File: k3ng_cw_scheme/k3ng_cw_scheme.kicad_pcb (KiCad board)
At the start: 2 copper layers, 100 x 116.8 mm, 35 parts, among them J1 INPUT KEY, J2 OUTPUT KEY/PTT, SW1 CMD, SW2 MEM1, SW3 MEM2, SW4 MEM3, SW5 MEM4, U1 PC817, U2 PC817

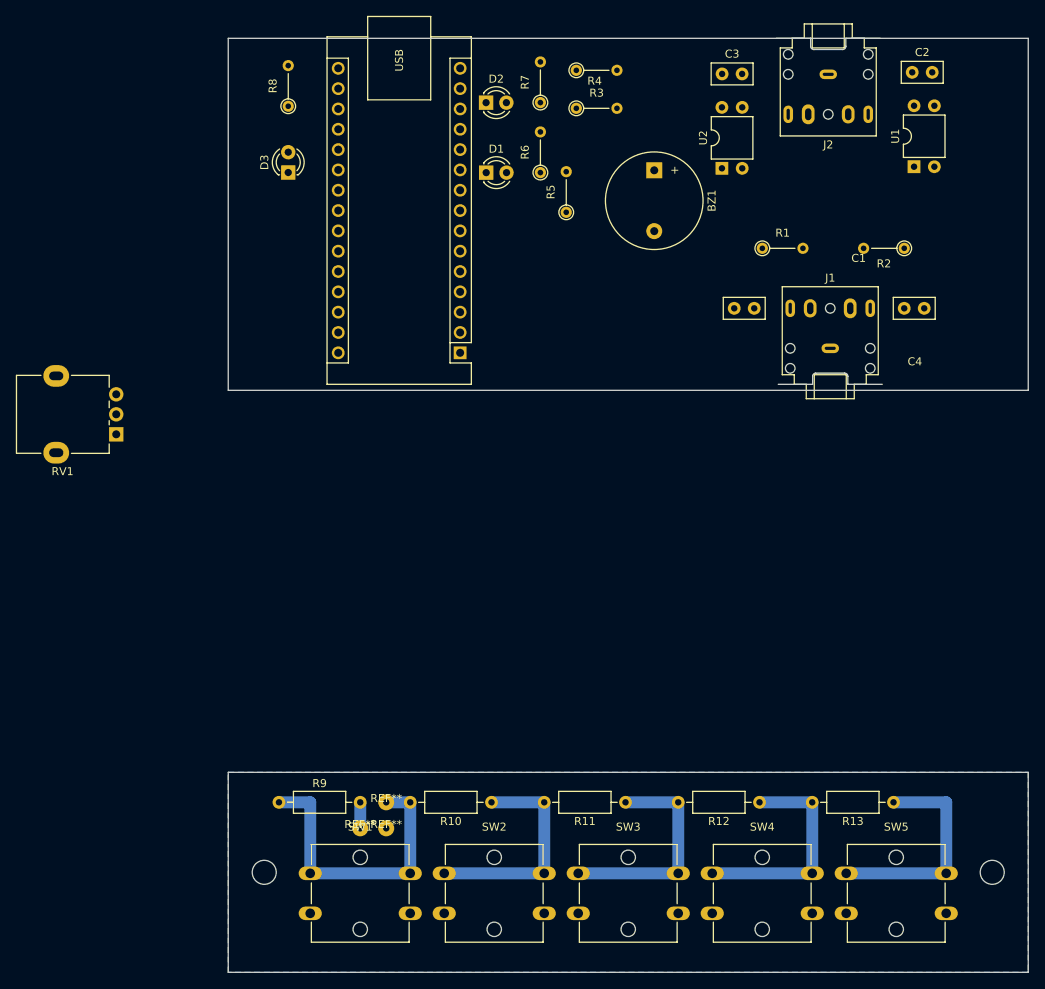
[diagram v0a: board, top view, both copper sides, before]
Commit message: Add keyboard connector Start working on PCB
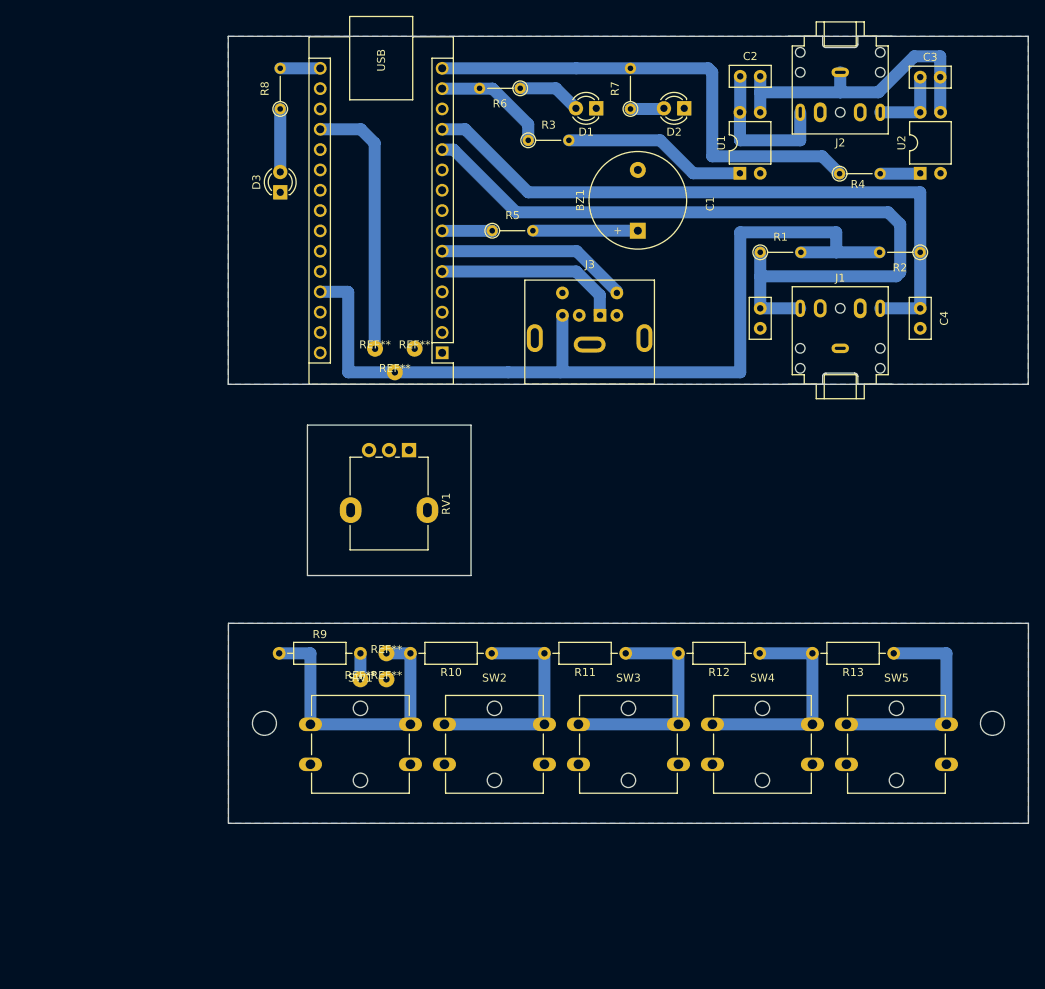
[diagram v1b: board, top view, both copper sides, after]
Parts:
- added J3: Keyboard, Footprints:Connector_Mini-DIN_Female_6Pin_2rows, F.Cu at (93.2, 98.6)
- added REF**: my_pad, my_lib:my_pad, F.Cu at (67.6, 105.8)
- added REF**: my_pad, my_lib:my_pad, F.Cu at (70.0, 102.8)
- added REF**: my_pad, my_lib:my_pad, F.Cu at (65.1, 102.8)
- moved RV1 36.7 mm to (69.3, 115.5), turned to -90 degrees
- moved R4 35.4 mm to (123.2, 80.9)
- moved U2 24.8 mm to (133.2, 80.9)
- moved D2 24.8 mm to (103.8, 72.8), turned to 180 degrees
- moved C3 24.8 mm to (133.2, 68.8)
- moved U1 21.8 mm to (110.7, 80.9)
- moved C2 21.5 mm to (110.8, 68.8)
- moved R10 18.6 mm to (79.7, 140.9)
- moved R11 18.6 mm to (96.4, 140.9)
- moved R12 18.6 mm to (113.2, 140.9)
- moved R13 18.6 mm to (129.9, 140.9)
- moved R9 18.6 mm to (53.1, 140.9)
- moved REF** 18.6 mm to (66.5, 144.1)
- moved REF** 18.6 mm to (66.5, 140.9)
- moved REF** 18.6 mm to (63.3, 144.1)
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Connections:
- A1 pad 11: unconnected-(A1-D8-Pad11) -> Net-(A1-D8)
- A1 pad 12: unconnected-(A1-D9-Pad12) -> Net-(A1-D9)
- C1 pad 1: Net-(A1-D3) -> Net-(A1-D8)
- C4 pad 1: Net-(A1-D2) -> Net-(A1-D9)
- J1 pad R: Net-(A1-D3) -> Net-(A1-D8)
- J1 pad T: Net-(A1-D2) -> Net-(A1-D9)
- J2 pad R: Net-(C2-Pad1) -> Net-(C3-Pad1)
- J2 pad T: Net-(C3-Pad1) -> Net-(C2-Pad1)
- R1 pad 1: Net-(A1-D3) -> Net-(A1-D8)
- R2 pad 1: Net-(A1-D2) -> Net-(A1-D9)
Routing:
- net +5V: track 3.25 -> 114.5 mm
- net Net-(A1-D8): track 0.00 -> 96.8 mm
- net Net-(A1-D9): track 0.00 -> 82.5 mm
- net Net-(A1-D12): track 0.00 -> 61.3 mm
- net Net-(C2-Pad2): track 0.00 -> 38.4 mm
- net Net-(A1-A0): track 0.00 -> 33.2 mm
- net Net-(A1-D3): track 0.00 -> 24.1 mm
- net Net-(A1-D2): track 0.00 -> 23.5 mm
- net Net-(R3-Pad2): track 0.00 -> 23.1 mm
- net Net-(C2-Pad1): track 0.00 -> 19.0 mm
- net Net-(A1-D11): track 0.00 -> 14.6 mm
- net Net-(BZ1-+): track 0.00 -> 13.1 mm
- net Net-(C3-Pad1): track 0.00 -> 9.40 mm
- net Net-(D1-A): track 0.00 -> 8.00 mm
- net Net-(D3-A): track 0.00 -> 7.88 mm
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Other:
- board size 100 x 116.8 mm -> 100 x 98.4 mm

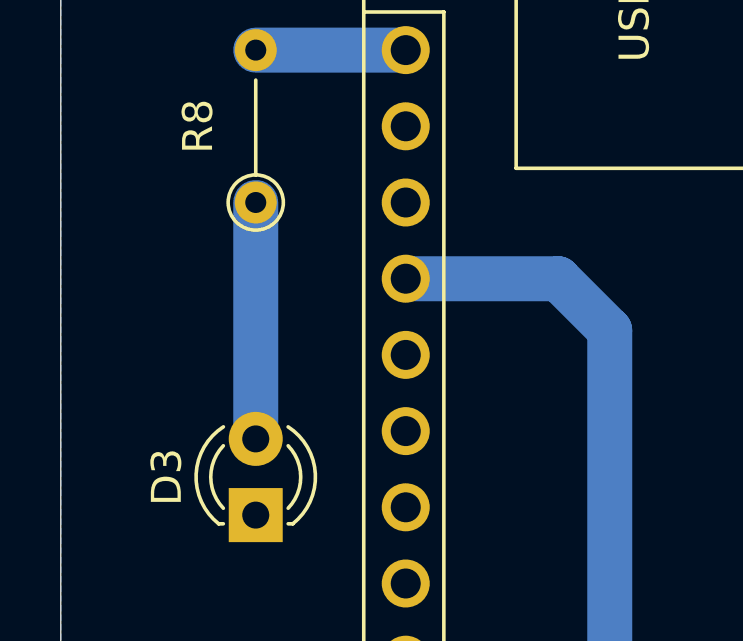
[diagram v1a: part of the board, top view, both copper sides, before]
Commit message: Add some pads to pcb
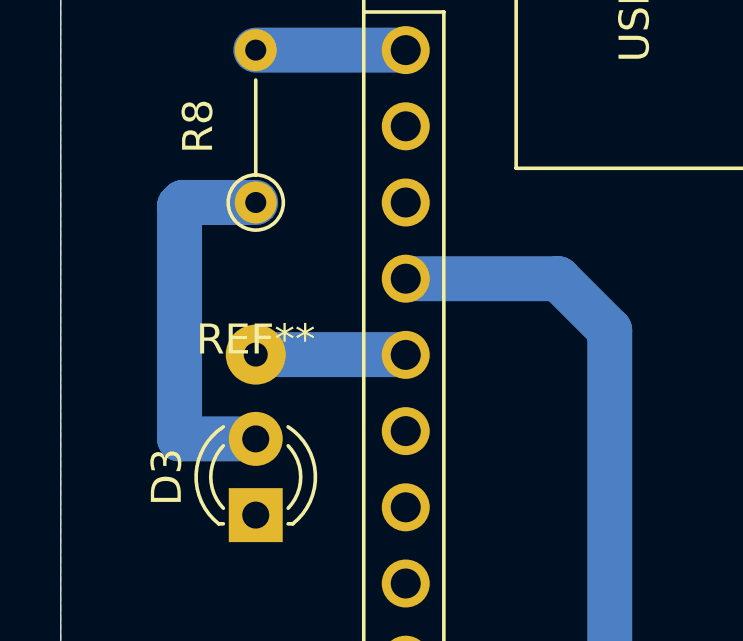
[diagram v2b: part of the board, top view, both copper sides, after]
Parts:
- added REF**: my_pad, my_lib:my_pad, F.Cu at (53.2, 77.9)
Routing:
- net Net-(D3-A): track 7.88 -> 12.9 mm
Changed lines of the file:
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@@
 		)
 	)
+	(footprint "my_lib:my_pad"
+		(layer "F.Cu")
+		(at 53.25 77.9)
+		(property "Reference" "REF**"
+			(at 0 -0.5 0)
+			(unlocked yes)
+			(layer "F.SilkS")
+			(effects
+				(font
+					(size 1 1)
+					(thickness 0.1)
+				)
+			)
+		)
+		(property "Value" "my_pad"
+			(at 0 1 0)
+			(unlocked yes)
+			(layer "F.Fab")
+			(effects
+				(font
+					(size 1 1)
+					(thickness 0.15)
+				)
+			)
+		)
+		(property "Datasheet" ""
+			(at 0 0 0)
+			(unlocked yes)
+			(layer "F.Fab")
+			(hide yes)
+			(effects
+				(font
+					(size 1 1)
+					(thickness 0.15)
+				)
+			)
+		)
+		(property "Description" ""
+			(at 0 0 0)
+			(unlocked yes)
+			(layer "F.Fab")
+			(hide yes)
+			(effects
+				(font
+					(size 1 1)
+					(thickness 0.15)
+				)
+			)
+		)
+		(attr smd)
+		(fp_text user "${REFERENCE}"
+			(at 0 2.5 0)
+			(unlocked yes)
+			(layer "F.Fab")
+			(effects
+				(font
+					(size 1 1)
+					(thickness 0.15)
+				)
+			)
+		)
+		(pad "1" thru_hole circle
+			(at 0 0)
+			(size 2 2)
+			(drill 0.8)
+			(layers "*.Cu" "*.Mask")
+			(remove_unused_layers no)
+			(net 39 "/A1")
+		)
+		(embedded_fonts no)
+	)
 	(footprint "Resistor_THT:R_Axial_DIN0207_L6.3mm_D2.5mm_P10.16mm_Horizontal"
 		(layer "F.Cu")
@@
 		)
 	)
+	(gr_line
+		(start 58.25 77.9)
+		(end 53.2 77.9)
+		(stroke
+			(width 1.5)
+			(type solid)
+		)
+		(layer "B.Cu")
+		(net 39)
+	)
 	(gr_circle
 		(center 142.275 149.625)
@@
 	)
 	(segment
+		(start 53.25 80.71)
+		(end 50.71 80.71)
+		(width 1.5)
+		(layer "B.Cu")
+		(net 32)
+	)
+	(segment
+		(start 50.82 72.83)
+		(end 50.71 72.94)
+		(width 1.5)
+		(layer "B.Cu")
+		(net 32)
+	)
+	(segment
+		(start 50.71 72.94)
+		(end 50.71 80.71)
+		(width 1.5)
+		(layer "B.Cu")
+		(net 32)
+	)
+	(segment
 		(start 53.25 72.83)
-		(end 53.25 80.71)
+		(end 50.82 72.83)
 		(width 1.5)
 		(layer "B.Cu")
